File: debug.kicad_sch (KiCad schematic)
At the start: 5 parts, among them J1 61300311121, J2 61300511121, J4 61300311121, J5 61300311121

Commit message: Silkscreen overlap a plated through-hole
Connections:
- net CAN_H_Debug renamed CAN_Debug_P
- net CAN_L_Debug renamed CAN_Debug_N
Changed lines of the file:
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@@
 		)
 	)
-	(hierarchical_label "CAN_H_Debug"
+	(hierarchical_label "CAN_Debug_P"
 		(shape bidirectional)
 		(at 154.94 97.79 180)
@@
 		)
 	)
-	(hierarchical_label "CAN_L_Debug"
+	(hierarchical_label "CAN_Debug_N"
 		(shape bidirectional)
 		(at 154.94 105.41 180)

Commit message: Reset components indexing
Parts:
- renumbered J1 to J2, J2 to J3, R19 to R24
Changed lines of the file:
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@@
 		(in_pos_files yes)
 		(dnp no)
-		(property "Reference" "R19"
+		(property "Reference" "R24"
 			(at 162.052 102.616 0)
 			(show_name no)
@@
 			(project "weather-station-poc"
 				(path "/38eb53bb-294e-46e4-ad59-fd355ca373b9/8a588a02-5ba4-4712-b770-7d9eb4e5d127"
-					(reference "R19")
+					(reference "R24")
 					(unit 1)
 				)
@@
 		(dnp no)
 		(fields_autoplaced yes)
-		(property "Reference" "J1"
+		(property "Reference" "J2"
 			(at 129.54 82.5499 0)
 			(show_name no)
@@
 			(project "weather-station-poc"
 				(path "/38eb53bb-294e-46e4-ad59-fd355ca373b9/8a588a02-5ba4-4712-b770-7d9eb4e5d127"
-					(reference "J1")
+					(reference "J2")
 					(unit 1)
 				)
@@
 		(dnp no)
 		(fields_autoplaced yes)
-		(property "Reference" "J2"
+		(property "Reference" "J3"
 			(at 129.54 100.3299 0)
 			(show_name no)
@@
 			(project "weather-station-poc"
 				(path "/38eb53bb-294e-46e4-ad59-fd355ca373b9/8a588a02-5ba4-4712-b770-7d9eb4e5d127"
-					(reference "J2")
+					(reference "J3")
 					(unit 1)
 				)
@@
 		(dnp no)
 		(fields_autoplaced yes)
-		(property "Reference" "#PWR0117"
+		(property "Reference" "#PWR0125"
 			(at 166.37 111.76 0)
 			(hide yes)
@@
 			(project "weather-station-poc"
 				(path "/38eb53bb-294e-46e4-ad59-fd355ca373b9/8a588a02-5ba4-4712-b770-7d9eb4e5d127"
-					(reference "#PWR0117")
+					(reference "#PWR0125")
 					(unit 1)
 				)
@@
 		(dnp no)
 		(fields_autoplaced yes)
-		(property "Reference" "#PWR0114"
+		(property "Reference" "#PWR0123"
 			(at 113.03 113.03 0)
 			(hide yes)
@@
 			(project "weather-station-poc"
 				(path "/38eb53bb-294e-46e4-ad59-fd355ca373b9/8a588a02-5ba4-4712-b770-7d9eb4e5d127"
-					(reference "#PWR0114")
+					(reference "#PWR0123")
 					(unit 1)
 				)
@@
 		(dnp no)
 		(fields_autoplaced yes)
-		(property "Reference" "#PWR0116"
+		(property "Reference" "#PWR0124"
 			(at 153.67 92.71 0)
 			(hide yes)
@@
 			(project "weather-station-poc"
 				(path "/38eb53bb-294e-46e4-ad59-fd355ca373b9/8a588a02-5ba4-4712-b770-7d9eb4e5d127"
-					(reference "#PWR0116")
+					(reference "#PWR0124")
 					(unit 1)
 				)
@@
 		(dnp no)
 		(fields_autoplaced yes)
-		(property "Reference" "#PWR0113"
+		(property "Reference" "#PWR0122"
 			(at 113.03 92.71 0)
 			(hide yes)
@@
 			(project "weather-station-poc"
 				(path "/38eb53bb-294e-46e4-ad59-fd355ca373b9/8a588a02-5ba4-4712-b770-7d9eb4e5d127"
-					(reference "#PWR0113")
+					(reference "#PWR0122")
 					(unit 1)
 				)

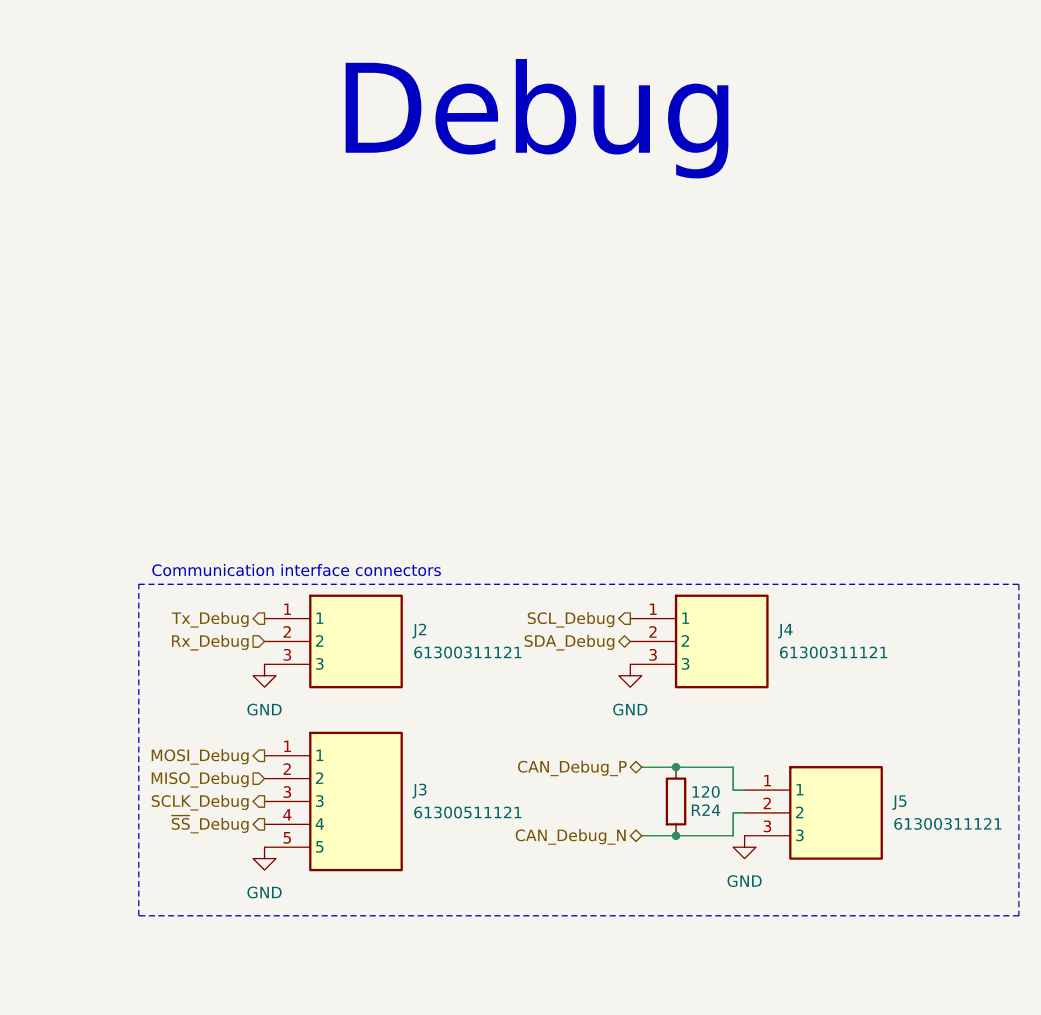
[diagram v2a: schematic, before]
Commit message: End of LCD signals routing
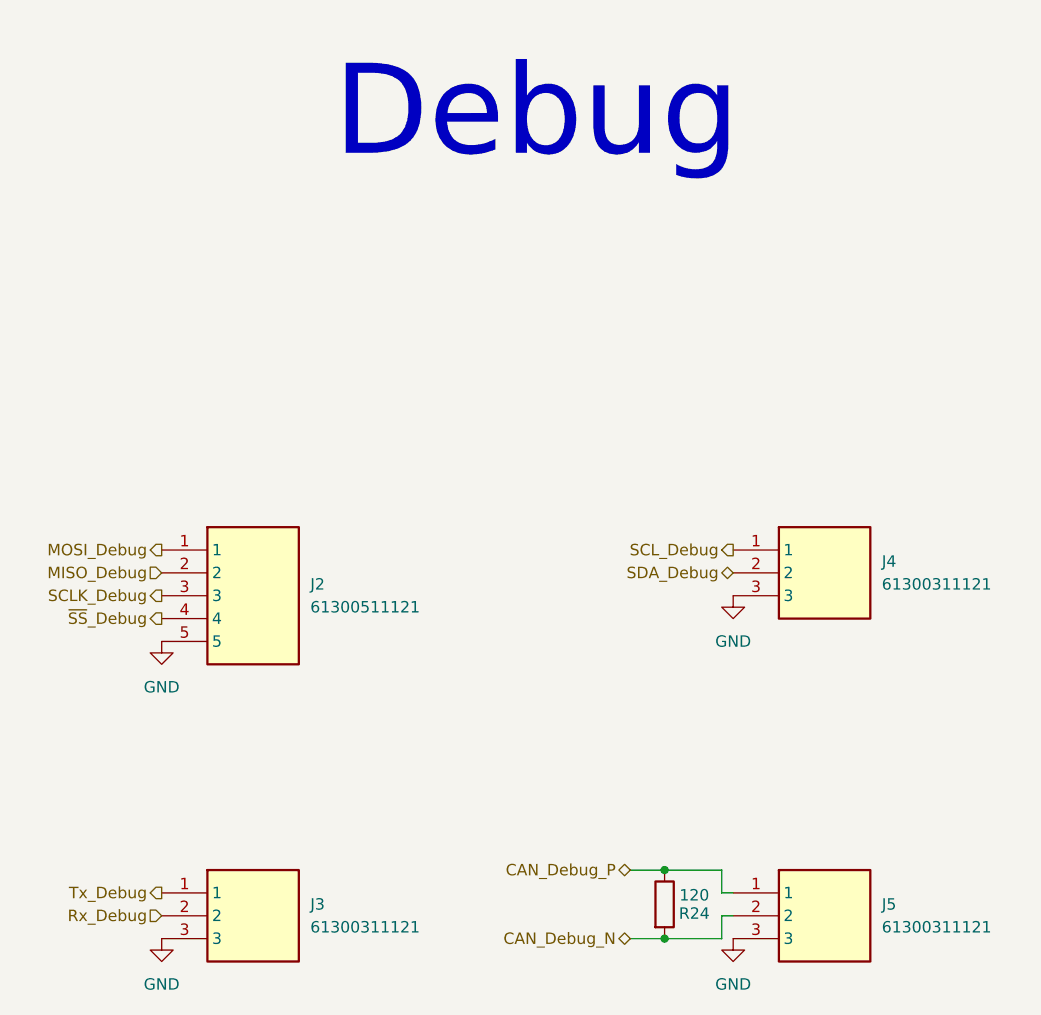
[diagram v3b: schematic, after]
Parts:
- renumbered J3 to J2, J2 to J3
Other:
- note removed: "Communication interface connectors"
- moved on the sheet: J2, J3, J4, J5, R24

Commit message: End of trace routing
Missing power plane on layer 2
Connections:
- net MISO_Debug: now also J2.3; no longer J2.2
- net MOSI_Debug: now also J2.2; no longer J2.1
- net SCLK_Debug: now also J2.4; no longer J2.3
- net ~{SS}_Debug: now also J2.1; no longer J2.4
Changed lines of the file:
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@@
 	(hierarchical_label "~{SS}_Debug"
 		(shape output)
-		(at 101.6 81.28 180)
+		(at 101.6 73.66 180)
 		(effects
 			(font
@@
 	(hierarchical_label "MOSI_Debug"
 		(shape output)
-		(at 101.6 73.66 180)
+		(at 101.6 76.2 180)
 		(effects
 			(font
@@
 	(hierarchical_label "SCLK_Debug"
 		(shape output)
-		(at 101.6 78.74 180)
+		(at 101.6 81.28 180)
 		(effects
 			(font
@@
 	(hierarchical_label "MISO_Debug"
 		(shape input)
-		(at 101.6 76.2 180)
+		(at 101.6 78.74 180)
 		(effects
 			(font
